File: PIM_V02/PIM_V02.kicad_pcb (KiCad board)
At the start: 4 copper layers, 93 x 62 mm, 326 parts, among them J1 Conn_01x06, J10 Conn_02x08_Odd_Even, J11 Conn_01x02, J12 Conn_01x02, J13 Conn_01x02, J4 USB_C_Receptacle_USB2.0_14P, J5 Conn_01x04, J6 Conn_01x04, J8 Conn_01x02, J9 Conn_02x08_Odd_Even, Q1 SQJ407EP-T1_GE3, Q2 PMOS, Q3 PMOS, Q4 NMOS, Q5 2N7002, SW1 SW_Push, U1 TPS259541DSGR, U10 TPS62933, U11 AP2112K-3.3, U12 MP28167GQ-A-P, U13 MT29F1G01ABAFDWB-IT_F, U14 MB85RS256B, U15 ICE40UP5K-SG48I, U16 INA3221, U2 USBLC6-2SC6, U3 STM32H7A3VITx, U4 MCP2562FDT-E/SN, U5 MCP2562FDT-E/SN, U6 TPS62933, U7 TPS62933, U8 TPS62933, U9 TPS62933, Y1 Crystal_GND24_Small

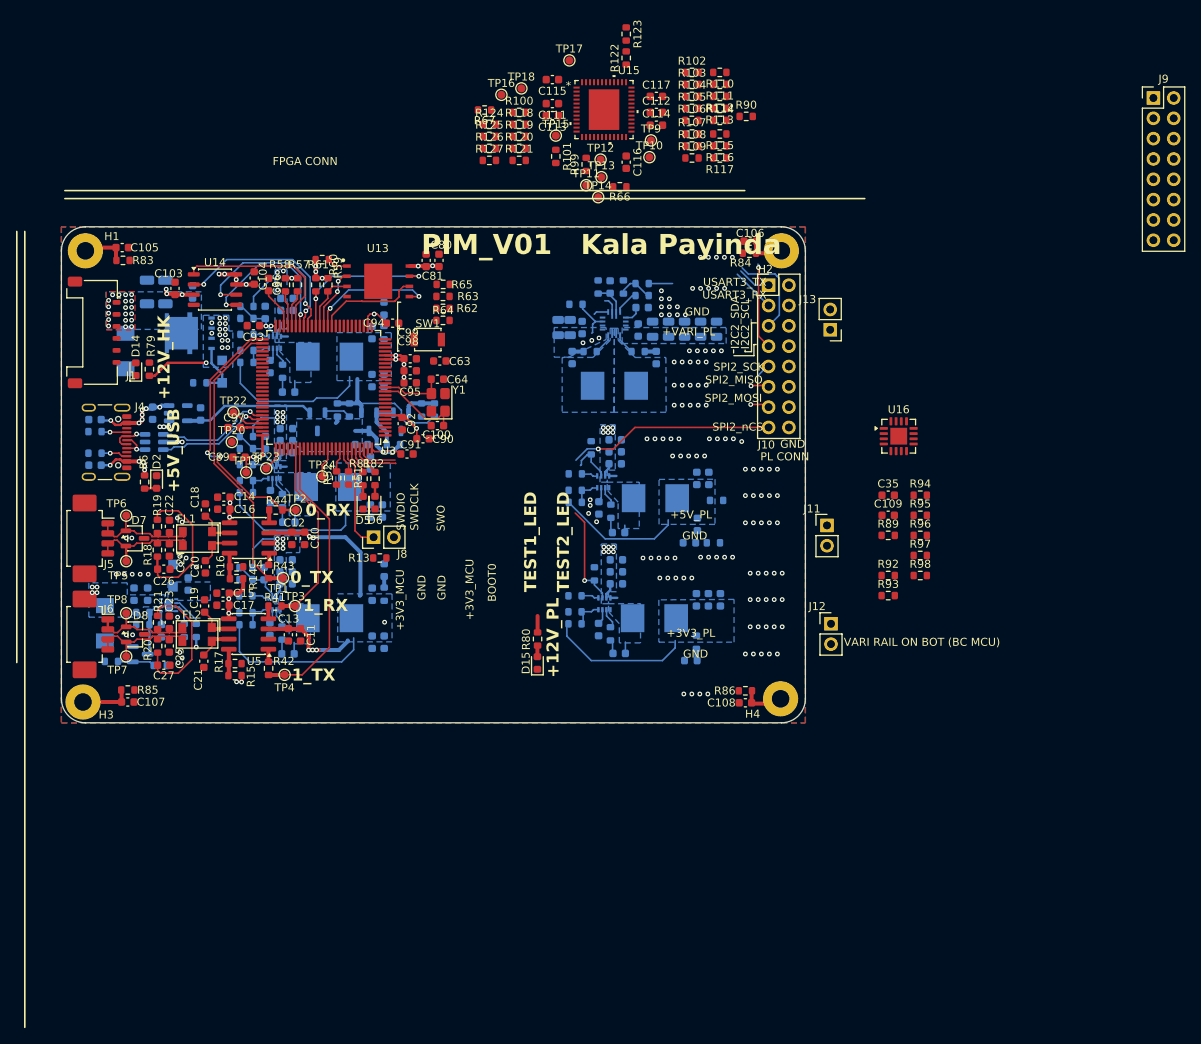
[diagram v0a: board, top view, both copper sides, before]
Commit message: pc104 outline, nearly done with layout, managed to keep it at 4 layers but the traces became quite messy; still need to do an in depth review to ensure i havent cut across any zones unknowingly; also there are still DRC errors that i need to work through - but all nets are connected !
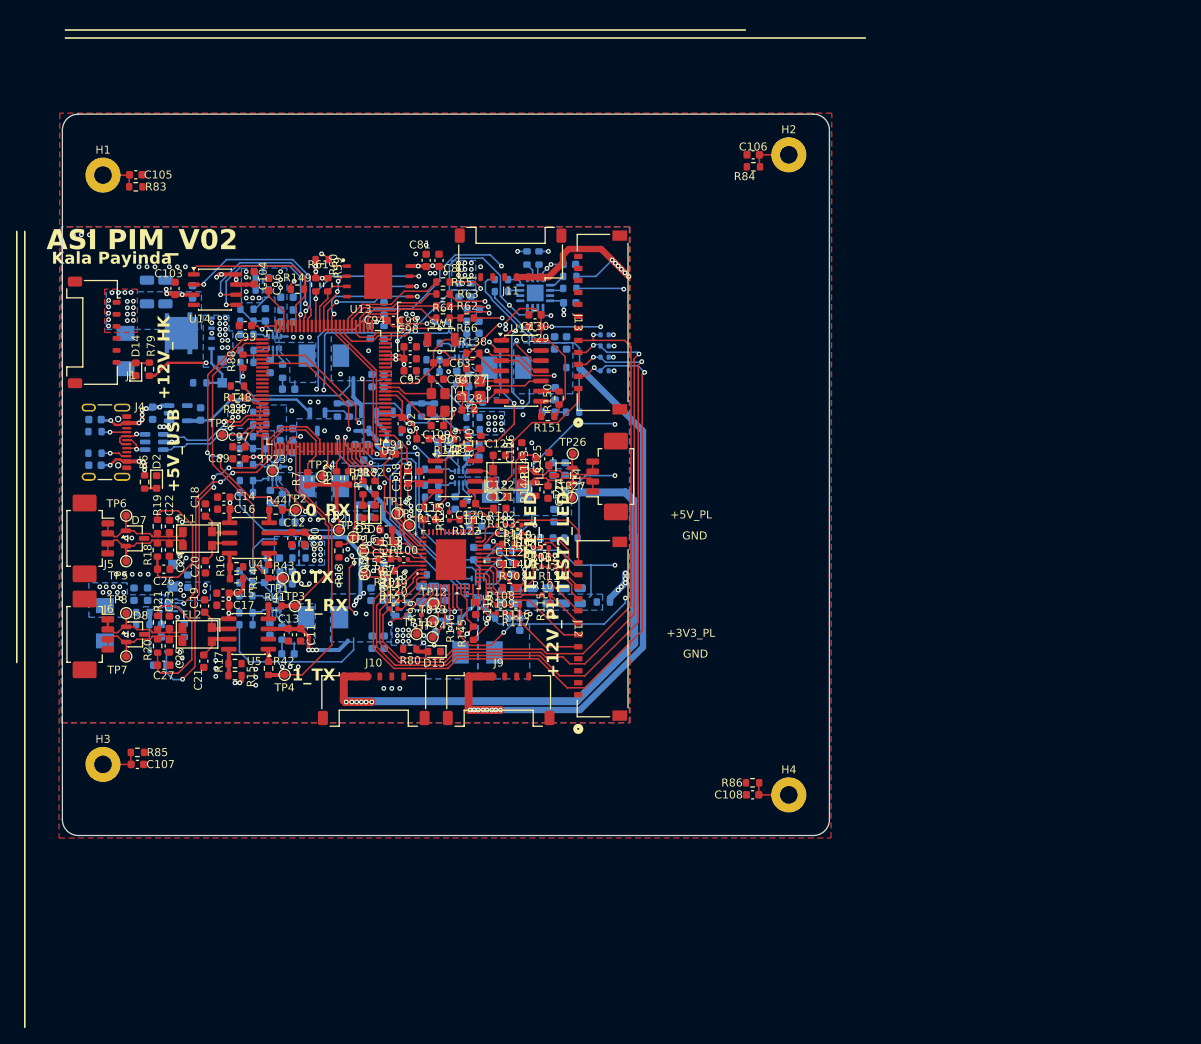
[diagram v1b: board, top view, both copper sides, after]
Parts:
- removed J8: Conn_01x02, Connector_PinHeader_2.54mm:PinHeader_1x02_P2.54mm_Vertical
- removed Q5: 2N7002, Package_TO_SOT_SMD:SOT-23
- removed TP10, TP19, TP20, TP9: TestPoint, TestPoint:TestPoint_Pad_D1.0mm
- added C110: 0.1uF, Capacitor_SMD:C_0603_1608Metric, B.Cu at (150.5, 60.7)
- added C118: 4.7uF, Capacitor_SMD:C_0603_1608Metric, F.Cu at (130.3, 87.3)
- added C119: 0.1uF, Capacitor_SMD:C_0603_1608Metric, F.Cu at (131.8, 87.3)
- added C120: 4.7uF, Capacitor_SMD:C_0603_1608Metric, F.Cu at (138.0, 90.6)
- added C121: 0.1uF, Capacitor_SMD:C_0603_1608Metric, F.Cu at (141.8, 91.2)
- added C122: 47pF, Capacitor_SMD:C_0603_1608Metric, F.Cu at (141.8, 89.7)
- added C123: 47pF, Capacitor_SMD:C_0603_1608Metric, F.Cu at (141.8, 84.6)
- added C124: 47pF, Capacitor_SMD:C_0603_1608Metric, F.Cu at (147.8, 89.2)
- added C125: 47pF, Capacitor_SMD:C_0603_1608Metric, F.Cu at (147.9, 85.0)
- added C126: 4.7nF, Capacitor_SMD:C_0603_1608Metric, F.Cu at (144.6, 83.8)
- added C127: 27pF, Capacitor_SMD:C_0603_1608Metric, F.Cu at (138.4, 73.7)
- added C128: 27pF, Capacitor_SMD:C_0603_1608Metric, F.Cu at (137.8, 78.9)
- added C129: 0.1uF, Capacitor_SMD:C_0603_1608Metric, F.Cu at (146.2, 68.5)
- added C130: 1uF, Capacitor_SMD:C_0603_1608Metric, F.Cu at (146.2, 67.0)
- added D16: BAS316, Diode_SMD:D_SOD-323, B.Cu at (99.1, 109.1)
- added D17: D_TVS_Dual_AAC, Package_TO_SOT_SMD:SOT-23-3, F.Cu at (149.7, 87.1)
- added FL3: Choke_CommonMode_FerriteCore_1243, Inductor_SMD:L_CommonModeChoke_Coilcraft_1812CAN, F.Cu at (142.8, 87.2)
- added J14: Conn_01x04, Connector_Molex:Molex_PicoBlade_53261-0471_1x04-1MP_P1.25mm_Horizontal, F.Cu at (155.8, 87.2)
- added R128: 0R, Resistor_SMD:R_0603_1608Metric, B.Cu at (112.1, 62.4)
- added R129: 0R, Resistor_SMD:R_0603_1608Metric, B.Cu at (112.1, 63.9)
- added R130: 0R, Resistor_SMD:R_0603_1608Metric, B.Cu at (111.8, 80.7)
- added R131: 0R, Resistor_SMD:R_0603_1608Metric, B.Cu at (111.8, 79.2)
- added R132: 0R, Resistor_SMD:R_0603_1608Metric, B.Cu at (136.7, 63.9)
- added R133: 0R, Resistor_SMD:R_0603_1608Metric, B.Cu at (138.2, 63.9)
- added R134: 0R, Resistor_SMD:R_0603_1608Metric, B.Cu at (138.4, 79.8)
- added R135: 0R, Resistor_SMD:R_0603_1608Metric, B.Cu at (138.5, 81.4)
- added R136: 0R, Resistor_SMD:R_0603_1608Metric, B.Cu at (128.8, 103.8)
- added R137: 0R, Resistor_SMD:R_0603_1608Metric, B.Cu at (130.3, 103.8)
- added R138: 10kR, Resistor_SMD:R_0603_1608Metric, F.Cu at (138.4, 71.8)
- added R139: 10kR, Resistor_SMD:R_0603_1608Metric, F.Cu at (137.8, 83.0)
- added R140: 0R, Resistor_SMD:R_0603_1608Metric, F.Cu at (139.4, 83.0)
- added R141: 1kR, Resistor_SMD:R_0603_1608Metric, F.Cu at (135.3, 82.5)
- added R142: 1kR, Resistor_SMD:R_0603_1608Metric, F.Cu at (133.2, 91.0)
- added R143: 60R, Resistor_SMD:R_0603_1608Metric, F.Cu at (146.3, 85.7)
- added R144: 60R, Resistor_SMD:R_0603_1608Metric, F.Cu at (146.3, 88.8)
- added R145: 10kR, Resistor_SMD:R_0603_1608Metric, F.Cu at (138.5, 106.8)
- added R146: 33R, Resistor_SMD:R_0402_1005Metric, F.Cu at (136.8, 106.2)
- added R147: 33R, Resistor_SMD:R_0603_1608Metric, F.Cu at (109.0, 77.4)
- added R148: 33R, Resistor_SMD:R_0603_1608Metric, F.Cu at (109.0, 75.9)
- added R149: 10kR, Resistor_SMD:R_0603_1608Metric, F.Cu at (116.5, 63.8)
- added R150: 10kR, Resistor_SMD:R_0603_1608Metric, F.Cu at (149.2, 77.4)
- added R151: 10kR, Resistor_SMD:R_0603_1608Metric, F.Cu at (147.8, 79.7)
- added TP21: TestPoint, TestPoint:TestPoint_Pad_D1.0mm, F.Cu at (121.7, 93.9)
- added TP25: TestPoint, TestPoint:TestPoint_Pad_D1.0mm, F.Cu at (123.5, 94.8)
- added TP26: TestPoint, TestPoint:TestPoint_Pad_D1.0mm, F.Cu at (150.9, 84.4)
- added TP27: TestPoint, TestPoint:TestPoint_Pad_D1.0mm, F.Cu at (150.8, 89.9)
- added U17: MCP2518FDT-E/SL, Package_SO:SOIC-14_3.9x8.7mm_P1.27mm, F.Cu at (144.5, 74.0)
- added U18: MCP2562FDT-E/SN, Package_SO:SOIC-8_3.9x4.9mm_P1.27mm, F.Cu at (136.2, 87.2)
- added Y2: Crystal_GND24_Small, Crystal:Crystal_SMD_Abracon_ABM8G-4Pin_3.2x2.5mm, F.Cu at (138.2, 76.2)
- C109, C35, R89, R92, R93, R94, R95, R96, R97, R98, U16: moved to B.Cu
- J10, J9: value Conn_02x08_Odd_Even -> Conn_01x06; footprint Connector_PinHeader_2.54mm:PinHeader_2x08_P2.54mm_Vertical -> CustomFootprints:Molex_Pico-Lock_504050-0691_1x06-1MP_P1.50mm_Horizontal
- J11: value Conn_01x02 -> Conn_01x06; footprint Connector_PinHeader_2.54mm:PinHeader_1x02_P2.54mm_Vertical -> CustomFootprints:Molex_Pico-Lock_504050-0691_1x06-1MP_P1.50mm_Horizontal
- J12, J13: value Conn_01x02 -> Conn_01x12; footprint Connector_PinHeader_2.54mm:PinHeader_1x02_P2.54mm_Vertical -> CustomFootprints:5040501291
- L1, L2, L3, L4, L5: value 6.8uH -> 2.2uF; footprint CustomFootprints:L_Wurth_WE-LHMI-7030 -> CustomFootprints:SRP5015TA-2R2M
- L6: value 4.7uH -> 2.2uF; footprint CustomFootprints:L_Wurth_WE-LHMI-7050 -> CustomFootprints:SRP5015TA-2R2M
- R100, R102, R103, R104, R105, R106, R107, R108, R109, R110, R111, R112, R113, R114, R115, R116, R117, R118, R119, R120, R121, R123, R99: footprint Resistor_SMD:R_0603_1608Metric -> Resistor_SMD:R_0402_1005Metric
- R124, R125, R126, R127: footprint Resistor_SMD:R_0603_1608Metric -> Resistor_SMD:R_0402_1005Metric; moved to B.Cu
- R57, R58: value 4.7kR -> 0R; moved to B.Cu
- R7: moved to F.Cu
- R87: value 1k -> 10kR
- R88: value 100k -> 10kR; moved to F.Cu
- U1: value TPS259541DSGR -> TPS259540DSGR
- moved J9 111.1 mm to (141.7, 115.0)
- moved C35 78.2 mm to (115.2, 67.9)
- moved J10 71.5 mm to (126.0, 115.0)
- moved R90 65.9 mm to (143.0, 101.1)
- moved R123 64.2 mm to (135.5, 92.2), turned to 90 degrees
- moved R116 62.8 mm to (143.8, 103.3)
- moved R115 62.8 mm to (148.1, 103.5), turned to 90 degrees
- moved R117 62.3 mm to (143.8, 104.3)
- moved R108 62.2 mm to (141.9, 103.3)
- moved R110 62.0 mm to (144.0, 93.3)
- moved R109 61.7 mm to (141.9, 104.3)
- moved R111 61.5 mm to (144.0, 94.3)
- moved TP17 61.4 mm to (130.5, 93.3)
- moved R102 61.4 mm to (142.0, 93.3)
- moved R122 61.1 mm to (137.6, 92.6), turned to 180 degrees
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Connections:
- net /EFUSE_EN renamed /EN_EF
- net /EFUSE_ENxxx renamed Net-(D16-A)
- net /nPL_FLT renamed /nFLT_EF
- C28 pad 1: +12V_HK -> Net-(U6-VIN)
- C29 pad 1: +12V_HK -> Net-(U7-VIN)
- C30 pad 1: +12V_HK -> Net-(U8-VIN)
- C31 pad 1: +12V_HK -> Net-(U6-VIN)
- C32 pad 1: +12V_HK -> Net-(U7-VIN)
- C33 pad 1: +12V_HK -> Net-(U8-VIN)
- C34 pad 1: +12V_HK -> Net-(U6-VIN)
- C35 pad 1: +12V_HK -> Net-(U7-VIN)
- C36 pad 1: +12V_HK -> Net-(U8-VIN)
- C49 pad 1: +12V_PL -> Net-(U9-VIN)
- C50 pad 1: +12V_PL -> Net-(U10-VIN)
- C51 pad 1: +12V_PL -> Net-(U9-VIN)
- C52 pad 1: +12V_PL -> Net-(U10-VIN)
- C53 pad 1: +12V_PL -> Net-(U9-VIN)
- C54 pad 1: +12V_PL -> Net-(U10-VIN)
- C68 pad 1: +12V_PL -> Net-(U12-IN)
- C69 pad 1: +12V_PL -> Net-(U12-IN)
- C70 pad 1: +12V_PL -> Net-(U12-IN)
- J10 pad 1: /USART3_TX_PL -> +3V3_PL
- J10 pad 2: GND -> +3V3_PL
- J10 pad 3: /USART3_RX_PL -> +3V3_PL
- J10 pad 5: /I2C2_SCL_PL -> GND
- J11 pad 1: +5V_PL -> +VARI_PL
- J11 pad 2: GND -> +VARI_PL
- J12 pad 1: +3V3_PL -> GND
- J13 pad 1: +VARI_PL -> /PL_IO8
- J13 pad 2: GND -> /PL_IO9
- J9 pad 1: +3V3_MCU -> +5V_PL
- J9 pad 2: GND -> +5V_PL
- J9 pad 3: /SPI1_SCK_FPGA -> +5V_PL
- J9 pad 5: /SPI1_MOSI_FPGA -> GND
- R123 pad 1: +3V3_HK -> /PL_IO8
- R123 pad 2: /PL_IO8 -> +3V3_HK
- R45 pad 1: +12V_HK -> Net-(U6-VIN)
- R47 pad 1: +12V_HK -> Net-(U7-VIN)
- R49 pad 1: +12V_HK -> Net-(U8-VIN)
- R57 pad 1: /I2C2_SCL_PL -> +12V_HK
- R57 pad 2: +3V3_MCU -> Net-(U6-VIN)
- R58 pad 1: +3V3_MCU -> +12V_HK
- R58 pad 2: /I2C2_SDA_PL -> Net-(U6-VIN)
- R59 pad 1: +3V3_MCU -> unconnected-(R59-Pad1)
- R59 pad 2: /OCTOSPI1_BK2_NCS -> unconnected-(R59-Pad2)
- R87 pad 2: Net-(Q5-G) -> GND
- R88 pad 1: Net-(Q5-G) -> +3V3_MCU
- R88 pad 2: GND -> /+VARI_ALT
- TP18 pad 1: /FPGA_EXTRA -> /FPGA_HB
- U10 pad 3: +12V_PL -> Net-(U10-VIN)
- U12 pad 1: +12V_PL -> Net-(U12-IN)
- U12 pad 4: unconnected-(U12-ALT-Pad4) -> /+VARI_ALT
- U15 pad 13: unconnected-(U15-IOB_24a-Pad13) -> /SPI_SCK_CAN2
- U15 pad 18: unconnected-(U15-IOB_31b-Pad18) -> /SPI_MOSI_CAN2
- U15 pad 19: unconnected-(U15-IOB_29b-Pad19) -> /SPI_MISO_CAN2
- U15 pad 20: unconnected-(U15-IOB_25b_G3-Pad20) -> Net-(U15-IOB_25b_G3)
- U15 pad 21: unconnected-(U15-IOB_23b-Pad21) -> /nSS_SPI_CAN2
- U15 pad 3: /FPGA_EXTRA -> /FPGA_HB
- U15 pad 4: unconnected-(U15-IOB_8a-Pad4) -> /FPGA_TXRDY
- U15 pad 6: unconnected-(U15-IOB_13b-Pad6) -> /nINT_CAN2
- U16 pad 16: unconnected-(U16-VPU-Pad16) -> +3V3_MCU
- U3 pad 35: /FPGA_EXTRA -> /FPGA_HB
- U3 pad 46: /I2C2_SCL_PL -> unconnected-(U3-PB10-Pad46)
- U3 pad 47: /I2C2_SDA_PL -> unconnected-(U3-PB11-Pad47)
- U3 pad 53: /SPI2_MISO_PL -> unconnected-(U3-PB14-Pad53)
- U3 pad 54: /SPI2_MOSI_PL -> unconnected-(U3-PB15-Pad54)
- U3 pad 55: /USART3_TX_PL -> /+VARI_ALT
- U3 pad 56: /USART3_RX_PL -> unconnected-(U3-PD9-Pad56)
- U3 pad 57: unconnected-(U3-PD10-Pad57) -> /FPGA_TXRDY
- U3 pad 63: unconnected-(U3-PC6-Pad63) -> /EXTRA_0
- U3 pad 64: unconnected-(U3-PC7-Pad64) -> /EXTRA_1
- U3 pad 66: unconnected-(U3-PC9-Pad66) -> Net-(U3-PC9)
- U3 pad 67: unconnected-(U3-PA8-Pad67) -> Net-(U3-PA8)
- U3 pad 84: /SPI2_SCK_PL -> unconnected-(U3-PD3-Pad84)
- U3 pad 85: /SPI2_nCS_PL -> unconnected-(U3-PD4-Pad85)
- U6 pad 3: +12V_HK -> Net-(U6-VIN)
- U7 pad 3: +12V_HK -> Net-(U7-VIN)
- U8 pad 3: +12V_HK -> Net-(U8-VIN)
- U9 pad 3: +12V_PL -> Net-(U9-VIN)
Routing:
- net +3V3_PL: track 0.00 -> 125.3 mm, vias 0 -> 8
- net +5V_PL: track 0.00 -> 96.4 mm, vias 0 -> 8
- net /PL_IO9: track 0.00 -> 90.4 mm, vias 0 -> 2
- net /POWER_SCL: track 4.85 -> 92.8 mm, vias 0 -> 4
- net /PL_IO10: track 0.00 -> 86.8 mm, vias 0 -> 2
- net /SPI1_MOSI_FPGA: track 0.00 -> 86.1 mm, vias 0 -> 2
- net /SPI_SCK_CAN2: track 0.00 -> 85.8 mm, vias 0 -> 2
- net /PL_IO11: track 0.00 -> 83.5 mm, vias 0 -> 2
- net /nSS_SPI_FPGA: track 0.00 -> 82.1 mm, vias 0 -> 2
- net /SPI1_SCK_FPGA: track 0.00 -> 81.9 mm, vias 0 -> 2
- net /POWER_SDA: track 5.37 -> 86.8 mm, vias 0 -> 4
- net /PL_IO12: track 0.00 -> 80.4 mm, vias 0 -> 1
- net /nSS_SPI_CAN2: track 0.00 -> 77.2 mm, vias 0 -> 2
- net /SPI_MISO_CAN2: track 0.00 -> 77.0 mm, vias 0 -> 2
- net /SPI_MOSI_CAN2: track 0.00 -> 74.8 mm, vias 0 -> 2
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- added copper zone on B.Cu, net /POWER/SUP_3V3_PL
- added copper zone on B.Cu, net /POWER/SUP_VARI_PL
- added copper zone on B.Cu, net Net-(U10-VIN)
- added copper zone on B.Cu, net Net-(U12-IN)
- added copper zone on B.Cu, net Net-(U6-VIN)
- added copper zone on B.Cu, net Net-(U7-VIN)
- added copper zone on B.Cu, net Net-(U8-VIN)
- added copper zone on B.Cu, net Net-(U9-VIN)
- removed copper zone on B.Cu, net +3V3_PL
- removed copper zone on B.Cu, net +VARI_PL
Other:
- board size 93 x 62 mm -> 95.9 x 90.2 mm
- board text added: "ASI PIM_V02"
- board text added: "Kala Payinda"
- board text removed: "+VARI_PL"
- board text removed: "FPGA CONN"
- board text removed: "I2C2_SCL"
- board text removed: "I2C2_SDA"
- board text removed: "PIM_V01 Kala Payinda"
- board text removed: "PL CONN"
- board text removed: "SPI2_MISO"
- board text removed: "SPI2_MOSI"
- board text removed: "SPI2_SCK"
- board text removed: "SPI2_nCS"
- board text removed: "SWDCLK"
- board text removed: "SWDIO"
- board text removed: "SWO"
- board text removed: "USART3_RX"
- board text removed: "USART3_TX"
- board text removed: "VARI RAIL ON BOT (BC MCU)"
